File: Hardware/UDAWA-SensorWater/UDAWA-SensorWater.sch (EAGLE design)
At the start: 7 parts

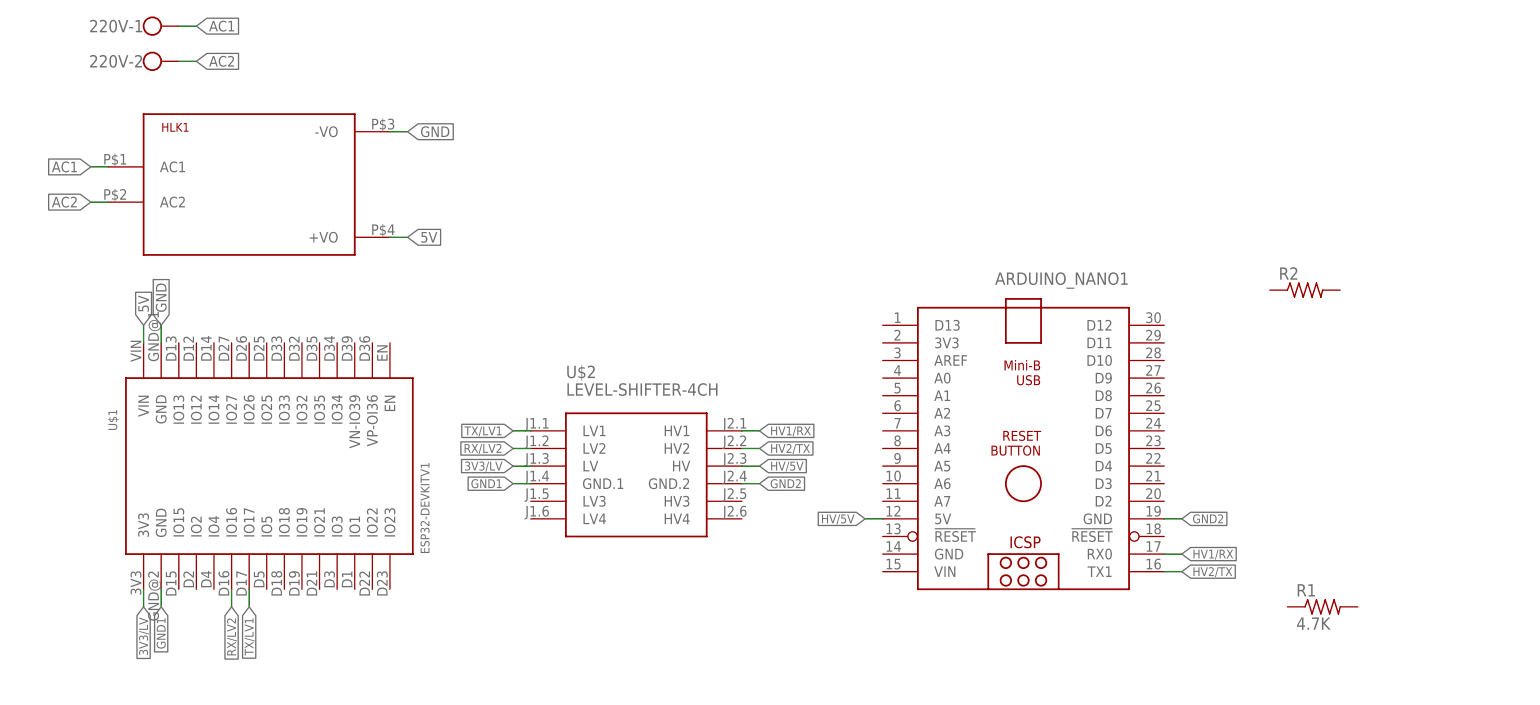
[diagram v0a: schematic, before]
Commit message: Menambahkan Terminal Block untuk koneksi ke Sensor TDS dan Sensor DS18B20 dan Wiring sesuai diagram di gambar #6
Menambahkan Terminal Block untuk koneksi ke Sensor TDS dan Sensor DS18B20 dan Wiring sesuai diagram di gambar #6
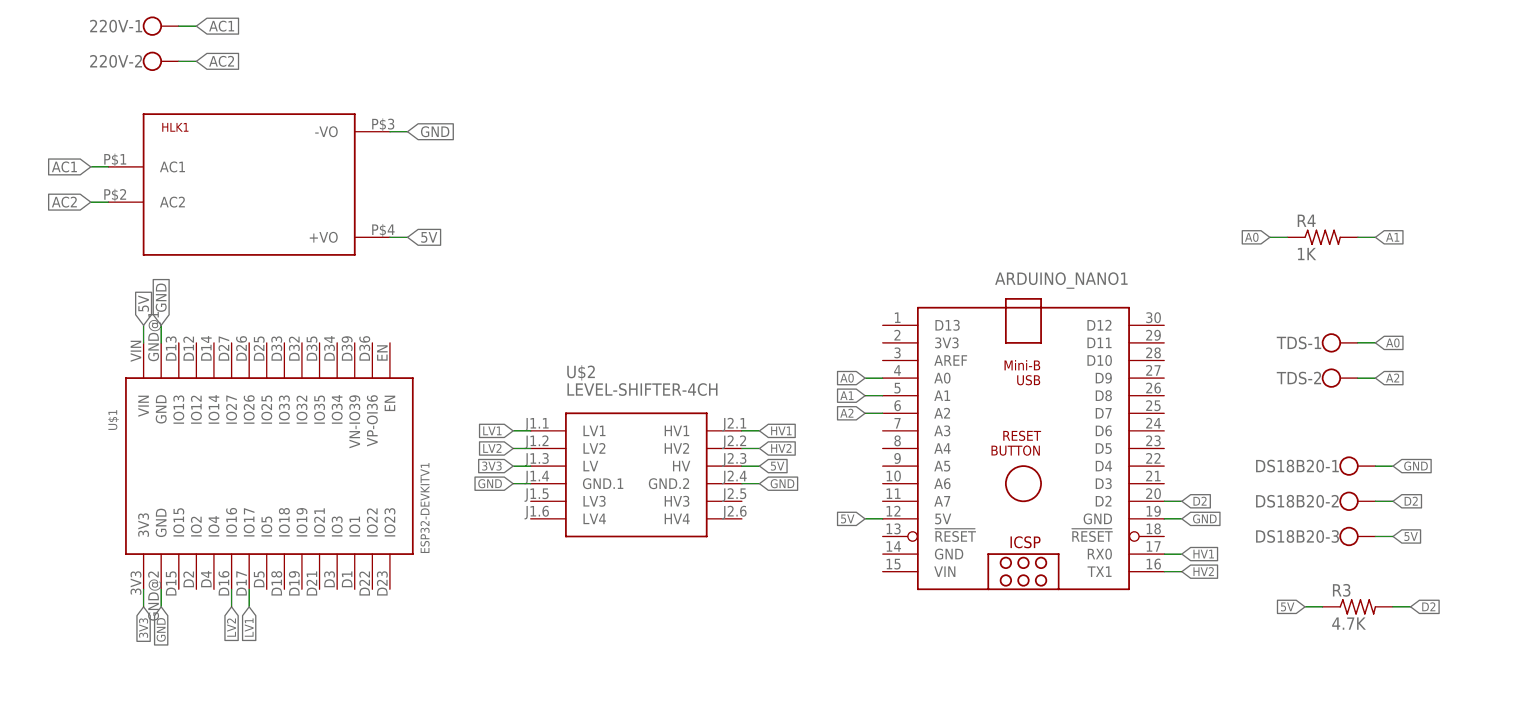
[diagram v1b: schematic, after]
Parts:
- removed R1: 4.7K, rcl:R-US_0207/12
- removed R2: (no value), rcl:R-US_0207/12
- added DS18B20: (no value), con-wago-500:W237-103
- added R3: 4.7K, rcl:R-US_0204/7
- added R4: 1K, rcl:R-US_0204/7
- added TDS: (no value), con-wago-500:W237-102
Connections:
- net 3V3/LV renamed 3V3
- net HV1/RX renamed HV1
- net HV2/TX renamed HV2
- net RX/LV2 renamed LV2
- net TX/LV1 renamed LV1
- removed net GND1: U$1.GND@2, U$2.GND.1
- removed net GND2: ARDUINO_NANO1.GND@1, U$2.GND.2
- removed net HV/5V: ARDUINO_NANO1.5V, U$2.HV
- new net A0: ARDUINO_NANO1.A0, R4.1, TDS-1.KL
- new net A1: ARDUINO_NANO1.A1, R4.2
- new net A2: ARDUINO_NANO1.A2, TDS-2.KL
- new net D2: ARDUINO_NANO1.D2, DS18B20-2.KL, R3.2
- net 5V: now also ARDUINO_NANO1.5V, DS18B20-3.KL, R3.1, U$2.HV
- net GND: now also ARDUINO_NANO1.GND@1, DS18B20-1.KL, U$1.GND@2, U$2.GND.1, U$2.GND.2

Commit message: Routing PCB #6
Routing PCB
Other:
- moved on the sheet: U$1
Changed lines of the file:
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@@
 </plain>
 <instances>
-<instance part="U$1" gate="G$1" x="-127" y="-35.56" smashed="yes">
-<attribute name="NAME" x="-153.67" y="-30.48" size="1.27" layer="95" rot="R90"/>
+<instance part="U$1" gate="G$1" x="-134.62" y="-33.02" smashed="yes" rot="R90">
+<attribute name="NAME" x="-139.7" y="-59.69" size="1.27" layer="95" rot="R180"/>
 </instance>
 <instance part="HLK1" gate="G$1" x="-134.62" y="5.08" smashed="yes">
@@
 <segment>
 <pinref part="U$1" gate="G$1" pin="GND@1"/>
-<wire x1="-147.32" y1="-17.78" x2="-147.32" y2="-15.24" width="0.1524" layer="91"/>
-<label x="-147.32" y="-15.24" size="1.524" layer="95" rot="R90" xref="yes"/>
+<wire x1="-152.4" y1="-53.34" x2="-160.02" y2="-53.34" width="0.1524" layer="91"/>
+<label x="-160.02" y="-53.34" size="1.524" layer="95" rot="R180" xref="yes"/>
 </segment>
 <segment>
 <pinref part="U$1" gate="G$1" pin="GND@2"/>
-<wire x1="-147.32" y1="-53.34" x2="-147.32" y2="-55.88" width="0.1524" layer="91"/>
-<label x="-147.32" y="-55.88" size="1.27" layer="95" rot="R270" xref="yes"/>
+<wire x1="-116.84" y1="-53.34" x2="-111.76" y2="-53.34" width="0.1524" layer="91"/>
+<label x="-111.76" y="-53.34" size="1.27" layer="95" xref="yes"/>
 </segment>
 <segment>
@@
 <segment>
 <pinref part="U$1" gate="G$1" pin="VIN"/>
-<wire x1="-149.86" y1="-17.78" x2="-149.86" y2="-15.24" width="0.1524" layer="91"/>
-<label x="-149.86" y="-15.24" size="1.524" layer="95" rot="R90" xref="yes"/>
+<wire x1="-152.4" y1="-55.88" x2="-160.02" y2="-55.88" width="0.1524" layer="91"/>
+<label x="-160.02" y="-55.88" size="1.524" layer="95" rot="R180" xref="yes"/>
 </segment>
 <segment>
@@
 <segment>
 <pinref part="U$1" gate="G$1" pin="IO17"/>
-<wire x1="-134.62" y1="-53.34" x2="-134.62" y2="-55.88" width="0.1524" layer="91"/>
-<label x="-134.62" y="-55.88" size="1.27" layer="95" rot="R270" xref="yes"/>
+<wire x1="-116.84" y1="-40.64" x2="-111.76" y2="-40.64" width="0.1524" layer="91"/>
+<label x="-111.76" y="-40.64" size="1.27" layer="95" xref="yes"/>
 </segment>
 </net>
@@
 <segment>
 <pinref part="U$1" gate="G$1" pin="IO16"/>
-<wire x1="-137.16" y1="-53.34" x2="-137.16" y2="-55.88" width="0.1524" layer="91"/>
-<label x="-137.16" y="-55.88" size="1.27" layer="95" rot="R270" xref="yes"/>
+<wire x1="-116.84" y1="-43.18" x2="-111.76" y2="-43.18" width="0.1524" layer="91"/>
+<label x="-111.76" y="-43.18" size="1.27" layer="95" xref="yes"/>
 </segment>
 </net>
@@
 <segment>
 <pinref part="U$1" gate="G$1" pin="3V3"/>
-<wire x1="-149.86" y1="-53.34" x2="-149.86" y2="-55.88" width="0.1524" layer="91"/>
-<label x="-149.86" y="-55.88" size="1.27" layer="95" rot="R270" xref="yes"/>
+<wire x1="-116.84" y1="-55.88" x2="-111.76" y2="-55.88" width="0.1524" layer="91"/>
+<label x="-111.76" y="-55.88" size="1.27" layer="95" xref="yes"/>
 </segment>
 </net>

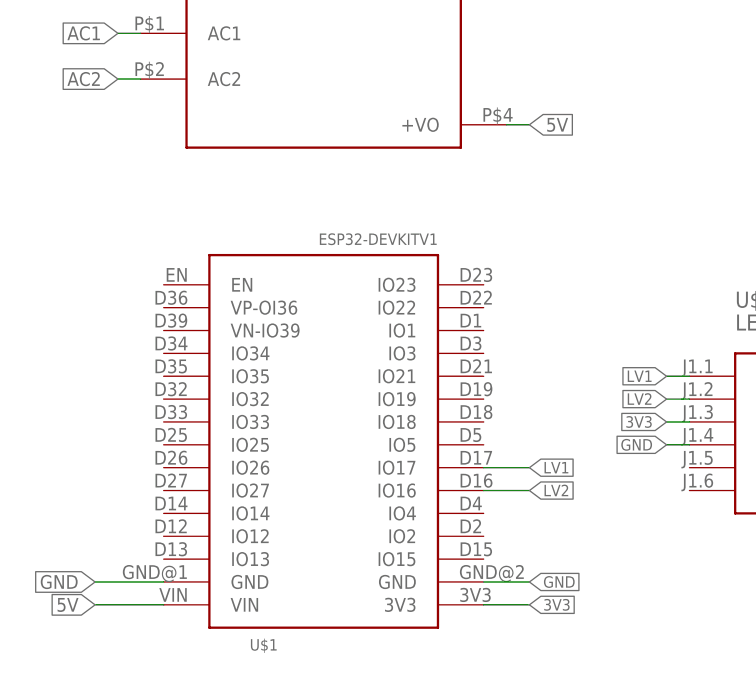
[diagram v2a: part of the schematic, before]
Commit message: Revert "Merge pull request #16 from NarinLab/sensor-water"
This reverts commit fa909a87a465dd37d6351bcf5a105db5a344029a, reversing
changes made to da9ed59faa8e6d8399543247dba95a3195e07114.

Conflict Error Fix
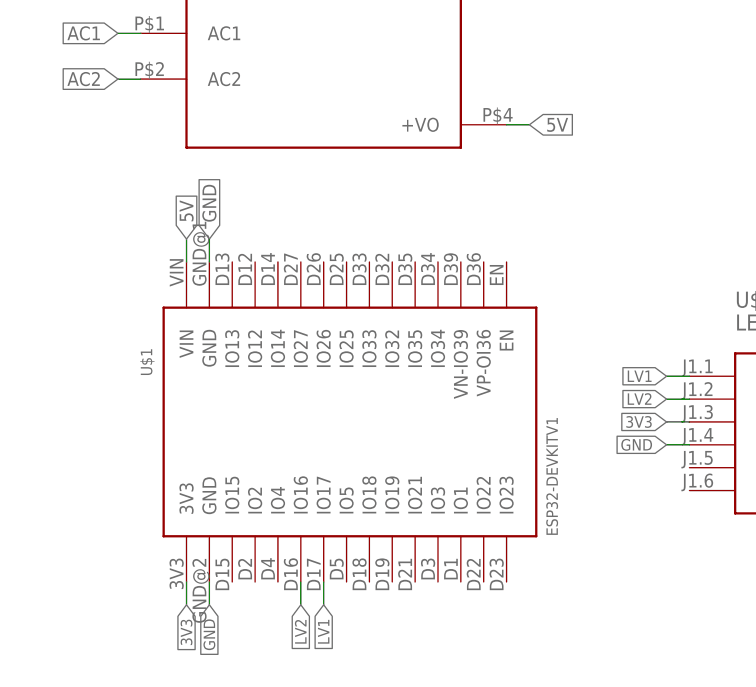
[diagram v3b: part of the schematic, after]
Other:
- moved on the sheet: U$1
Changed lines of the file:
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@@
 </plain>
 <instances>
-<instance part="U$1" gate="G$1" x="-134.62" y="-33.02" smashed="yes" rot="R90">
-<attribute name="NAME" x="-139.7" y="-59.69" size="1.27" layer="95" rot="R180"/>
+<instance part="U$1" gate="G$1" x="-127" y="-35.56" smashed="yes">
+<attribute name="NAME" x="-153.67" y="-30.48" size="1.27" layer="95" rot="R90"/>
 </instance>
 <instance part="HLK1" gate="G$1" x="-134.62" y="5.08" smashed="yes">
@@
 <segment>
 <pinref part="U$1" gate="G$1" pin="GND@1"/>
-<wire x1="-152.4" y1="-53.34" x2="-160.02" y2="-53.34" width="0.1524" layer="91"/>
-<label x="-160.02" y="-53.34" size="1.524" layer="95" rot="R180" xref="yes"/>
+<wire x1="-147.32" y1="-17.78" x2="-147.32" y2="-15.24" width="0.1524" layer="91"/>
+<label x="-147.32" y="-15.24" size="1.524" layer="95" rot="R90" xref="yes"/>
 </segment>
 <segment>
 <pinref part="U$1" gate="G$1" pin="GND@2"/>
-<wire x1="-116.84" y1="-53.34" x2="-111.76" y2="-53.34" width="0.1524" layer="91"/>
-<label x="-111.76" y="-53.34" size="1.27" layer="95" xref="yes"/>
+<wire x1="-147.32" y1="-53.34" x2="-147.32" y2="-55.88" width="0.1524" layer="91"/>
+<label x="-147.32" y="-55.88" size="1.27" layer="95" rot="R270" xref="yes"/>
 </segment>
 <segment>
@@
 <segment>
 <pinref part="U$1" gate="G$1" pin="VIN"/>
-<wire x1="-152.4" y1="-55.88" x2="-160.02" y2="-55.88" width="0.1524" layer="91"/>
-<label x="-160.02" y="-55.88" size="1.524" layer="95" rot="R180" xref="yes"/>
+<wire x1="-149.86" y1="-17.78" x2="-149.86" y2="-15.24" width="0.1524" layer="91"/>
+<label x="-149.86" y="-15.24" size="1.524" layer="95" rot="R90" xref="yes"/>
 </segment>
 <segment>
@@
 <segment>
 <pinref part="U$1" gate="G$1" pin="IO17"/>
-<wire x1="-116.84" y1="-40.64" x2="-111.76" y2="-40.64" width="0.1524" layer="91"/>
-<label x="-111.76" y="-40.64" size="1.27" layer="95" xref="yes"/>
+<wire x1="-134.62" y1="-53.34" x2="-134.62" y2="-55.88" width="0.1524" layer="91"/>
+<label x="-134.62" y="-55.88" size="1.27" layer="95" rot="R270" xref="yes"/>
 </segment>
 </net>
@@
 <segment>
 <pinref part="U$1" gate="G$1" pin="IO16"/>
-<wire x1="-116.84" y1="-43.18" x2="-111.76" y2="-43.18" width="0.1524" layer="91"/>
-<label x="-111.76" y="-43.18" size="1.27" layer="95" xref="yes"/>
+<wire x1="-137.16" y1="-53.34" x2="-137.16" y2="-55.88" width="0.1524" layer="91"/>
+<label x="-137.16" y="-55.88" size="1.27" layer="95" rot="R270" xref="yes"/>
 </segment>
 </net>
@@
 <segment>
 <pinref part="U$1" gate="G$1" pin="3V3"/>
-<wire x1="-116.84" y1="-55.88" x2="-111.76" y2="-55.88" width="0.1524" layer="91"/>
-<label x="-111.76" y="-55.88" size="1.27" layer="95" xref="yes"/>
+<wire x1="-149.86" y1="-53.34" x2="-149.86" y2="-55.88" width="0.1524" layer="91"/>
+<label x="-149.86" y="-55.88" size="1.27" layer="95" rot="R270" xref="yes"/>
 </segment>
 </net>
